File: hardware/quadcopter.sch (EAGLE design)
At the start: 61 parts, among them J1 AVR_SPI_PRG_6NS, J2 HEADER-4POS-2X2-0.1IN-FEMALE-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, J3 HEADER-10POSTH-254X10, J4 HEADER-4POS-0.1IN-FEMALE-SMD-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, Q1 MOSFET-SI2302CDS-T1-E3CT-ND, Q2 MOSFET-SI2302CDS-T1-E3CT-ND, Q3 MOSFET-SI2302CDS-T1-E3CT-ND, Q4 MOSFET-SI2302CDS-T1-E3CT-ND, Q5 MOSFET-SI2302CDS-T1-E3CT-ND, Q6 MOSFET-SI2302CDS-T1-E3CT-ND, SW1 PUSHBUTTON_SMD-VERTICAL-1, U1 ATMEGA128RFA1, U2 LSM-IMU-497-18367-1-NDIMU, Y1 CRYSTAL5X3

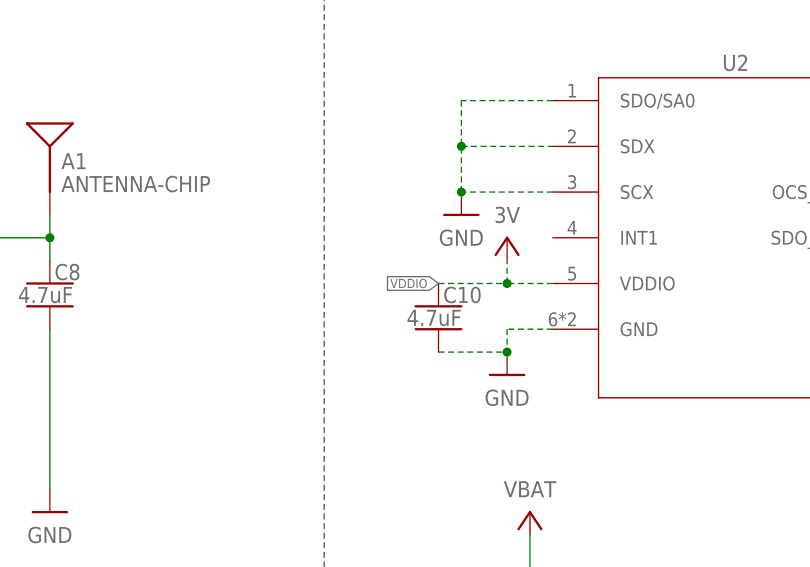
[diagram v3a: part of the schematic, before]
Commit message: switched gnd to gnd and removed VDDIO tag
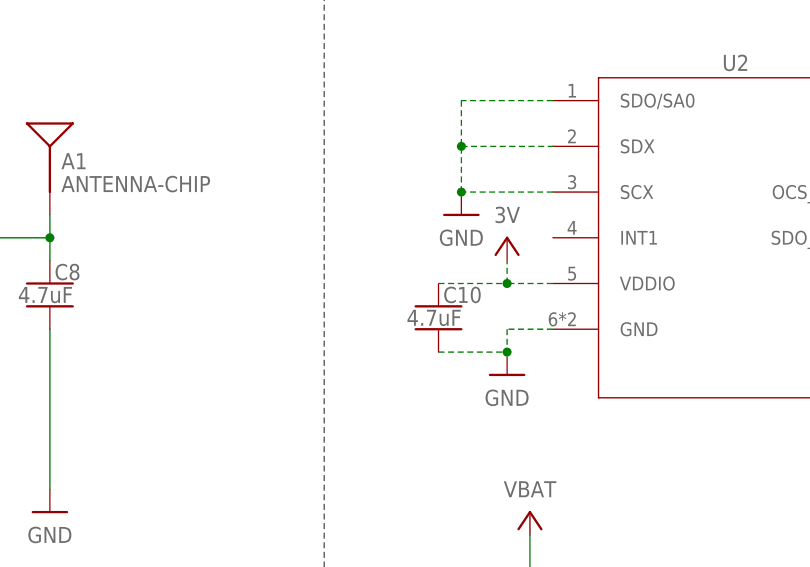
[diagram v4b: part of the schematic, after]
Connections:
- removed net GND1: C11.2
- net GND: now also C11.2
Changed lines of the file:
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@@
 <part name="P+7" library="quadparts_prebuilt_2022" deviceset="3V" device=""/>
 <part name="C10" library="quadparts_prebuilt_2022" deviceset="CAPACITOR-NP_" device="SMD-2012-0805_CERAMIC-4.7UF" value="4.7uF"/>
-<part name="GND19" library="quadparts_prebuilt_2022" deviceset="GND" device=""/>
 <part name="C11" library="quadparts_prebuilt_2022" deviceset="CAPACITOR-NP_" device="SMD-2012-0805_CERAMIC-4.7UF" value="4.7uF"/>
 <part name="R4" library="custom.lbr" library_urn="urn:adsk.wipprod:fs.file:vf.FjMADskDQ2Se9fX1PD5xcw" deviceset="MY-RESISTOR" device="-08050OHMRES" value="10k"/>
@@
 <part name="R12" library="custom.lbr" library_urn="urn:adsk.wipprod:fs.file:vf.FjMADskDQ2Se9fX1PD5xcw" deviceset="MY-RESISTOR" device="-08050OHMRES" value="2.2K"/>
 <part name="R14" library="custom.lbr" library_urn="urn:adsk.wipprod:fs.file:vf.FjMADskDQ2Se9fX1PD5xcw" deviceset="MY-RESISTOR" device="-08050OHMRES" value="2.2K"/>
+<part name="GND19" library="quadparts_prebuilt_2022" deviceset="GND" device=""/>
 </parts>
 <sheets>
@@
 <attribute name="NAME" x="229.108" y="150.241" size="1.778" layer="95"/>
 </instance>
-<instance part="GND19" gate="1" x="299.72" y="162.56" smashed="yes">
-<attribute name="VALUE" x="299.72" y="160.02" size="1.778" layer="96" align="center"/>
-</instance>
 <instance part="C11" gate="G$1" x="297.18" y="170.18" smashed="yes">
 <attribute name="VALUE" x="293.624" y="168.021" size="1.778" layer="96"/>
@@
 <attribute name="NAME" x="139.7" y="190.5" size="1.778" layer="95" rot="R90" align="bottom-center"/>
 <attribute name="VALUE" x="147.32" y="190.5" size="1.778" layer="96" rot="R90" align="bottom-center"/>
+</instance>
+<instance part="GND19" gate="1" x="299.72" y="162.56" smashed="yes">
+<attribute name="VALUE" x="299.72" y="160.02" size="1.778" layer="96" align="center"/>
 </instance>
 </instances>
@@
 <pinref part="C16" gate="G$1" pin="2"/>
 </segment>
+<segment>
+<wire x1="297.18" y1="165.1" x2="299.72" y2="165.1" width="0.1524" layer="91" style="longdash"/>
+<pinref part="C11" gate="G$1" pin="2"/>
+<pinref part="GND19" gate="1" pin="GND"/>
+</segment>
 </net>
 <net name="PG1" class="0">
@@
 </segment>
 </net>
-<net name="GND1" class="0">
-<segment>
-<wire x1="297.18" y1="165.1" x2="299.72" y2="165.1" width="0.1524" layer="91" style="longdash"/>
-<pinref part="GND19" gate="1" pin="GND"/>
-<pinref part="C11" gate="G$1" pin="2"/>
-</segment>
-</net>
 <net name="VDDIO" class="0">
 <segment>
@@
 <pinref part="P+5" gate="G$1" pin="3V"/>
 <wire x1="228.6" y1="152.4" x2="236.22" y2="152.4" width="0.1524" layer="91" style="longdash"/>
+<pinref part="C10" gate="G$1" pin="1"/>
 <junction x="236.22" y="152.4"/>
-<label x="228.6" y="152.4" size="1.016" layer="95" rot="R180" xref="yes"/>
-<pinref part="C10" gate="G$1" pin="1"/>
-</segment>
-<segment>
+</segment>
+<segment>

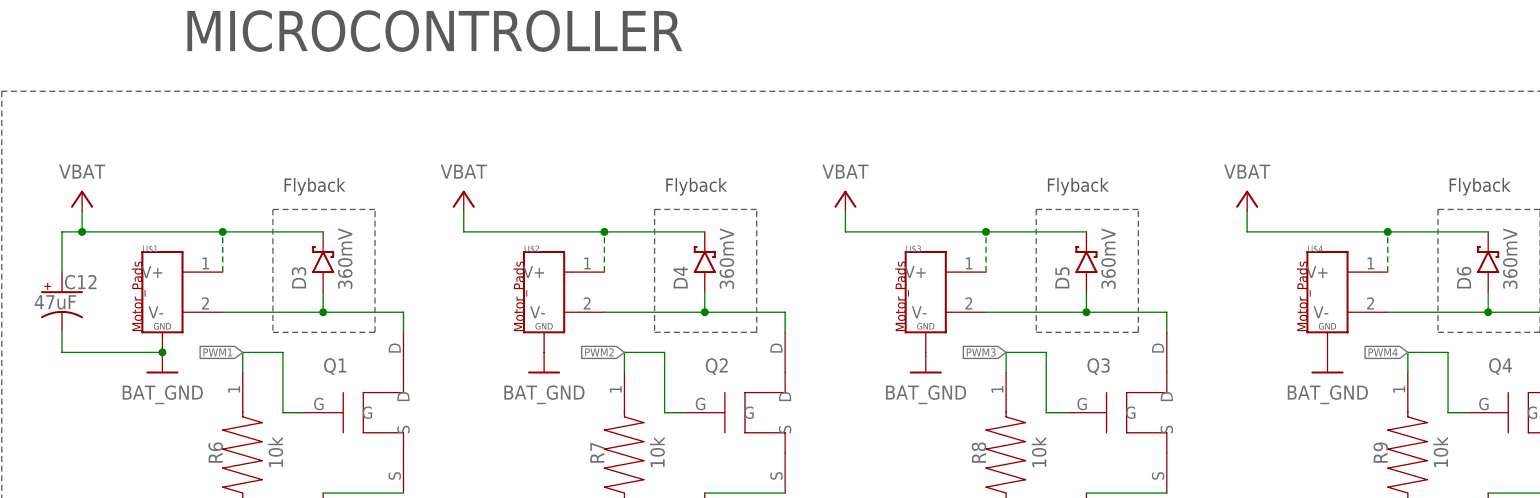
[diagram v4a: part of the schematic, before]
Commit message: renamed motors
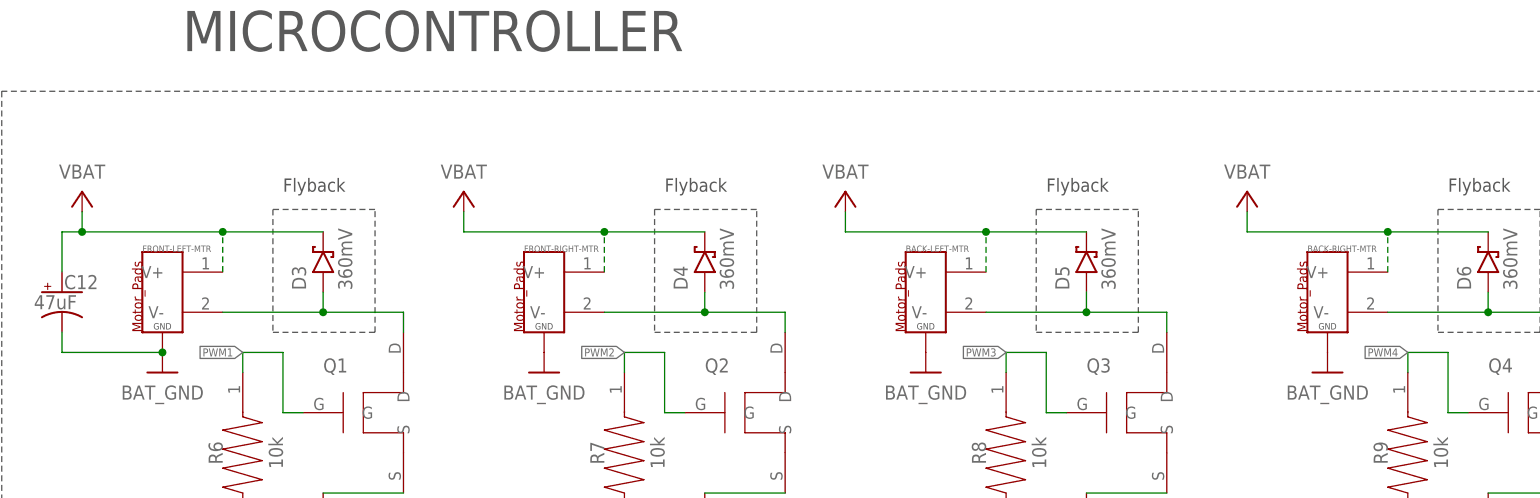
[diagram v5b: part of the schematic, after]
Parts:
- renumbered U$1 to FRONT-LEFT-MTR, U$2 to FRONT-RIGHT-MTR, U$3 to BACK-LEFT-MTR, U$4 to BACK-RIGHT-MTR
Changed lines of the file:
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@@
 <part name="R4" library="custom.lbr" library_urn="urn:adsk.wipprod:fs.file:vf.FjMADskDQ2Se9fX1PD5xcw" deviceset="MY-RESISTOR" device="-08050OHMRES" value="10k"/>
 <part name="R5" library="custom.lbr" library_urn="urn:adsk.wipprod:fs.file:vf.FjMADskDQ2Se9fX1PD5xcw" deviceset="MY-RESISTOR" device="-08050OHMRES" value="10k"/>
-<part name="U$1" library="quadparts_prebuilt_2022" deviceset="MOTOR_PADS_GND" device="-MOLEX-SMD"/>
+<part name="FRONT-LEFT-MTR" library="quadparts_prebuilt_2022" deviceset="MOTOR_PADS_GND" device="-MOLEX-SMD"/>
 <part name="P+8" library="quadparts_prebuilt_2022" deviceset="VBAT" device=""/>
 <part name="D3" library="quadparts_prebuilt_2022" deviceset="DIODE-SCHOTTKY_" device="-SMD-SOD123" package3d_urn="urn:adsk.eagle:package:11793366/1" value="360mV"/>
@@
 <part name="GND22" library="quadparts_prebuilt_2022" deviceset="GND" device=""/>
 <part name="Q1" library="custom.lbr" library_urn="urn:adsk.wipprod:fs.file:vf.FjMADskDQ2Se9fX1PD5xcw" deviceset="MOSFET" device="-SI2302CDS-T1-E3CT-ND"/>
-<part name="U$2" library="quadparts_prebuilt_2022" deviceset="MOTOR_PADS_GND" device="-MOLEX-SMD"/>
+<part name="FRONT-RIGHT-MTR" library="quadparts_prebuilt_2022" deviceset="MOTOR_PADS_GND" device="-MOLEX-SMD"/>
 <part name="P+9" library="quadparts_prebuilt_2022" deviceset="VBAT" device=""/>
 <part name="D4" library="quadparts_prebuilt_2022" deviceset="DIODE-SCHOTTKY_" device="-SMD-SOD123" package3d_urn="urn:adsk.eagle:package:11793366/1" value="360mV"/>
@@
 <part name="GND25" library="quadparts_prebuilt_2022" deviceset="GND" device=""/>
 <part name="Q2" library="custom.lbr" library_urn="urn:adsk.wipprod:fs.file:vf.FjMADskDQ2Se9fX1PD5xcw" deviceset="MOSFET" device="-SI2302CDS-T1-E3CT-ND"/>
-<part name="U$3" library="quadparts_prebuilt_2022" deviceset="MOTOR_PADS_GND" device="-MOLEX-SMD"/>
+<part name="BACK-LEFT-MTR" library="quadparts_prebuilt_2022" deviceset="MOTOR_PADS_GND" device="-MOLEX-SMD"/>
 <part name="P+10" library="quadparts_prebuilt_2022" deviceset="VBAT" device=""/>
 <part name="D5" library="quadparts_prebuilt_2022" deviceset="DIODE-SCHOTTKY_" device="-SMD-SOD123" package3d_urn="urn:adsk.eagle:package:11793366/1" value="360mV"/>
@@
 <part name="GND28" library="quadparts_prebuilt_2022" deviceset="GND" device=""/>
 <part name="Q3" library="custom.lbr" library_urn="urn:adsk.wipprod:fs.file:vf.FjMADskDQ2Se9fX1PD5xcw" deviceset="MOSFET" device="-SI2302CDS-T1-E3CT-ND"/>
-<part name="U$4" library="quadparts_prebuilt_2022" deviceset="MOTOR_PADS_GND" device="-MOLEX-SMD"/>
+<part name="BACK-RIGHT-MTR" library="quadparts_prebuilt_2022" deviceset="MOTOR_PADS_GND" device="-MOLEX-SMD"/>
 <part name="P+11" library="quadparts_prebuilt_2022" deviceset="VBAT" device=""/>
 <part name="D6" library="quadparts_prebuilt_2022" deviceset="DIODE-SCHOTTKY_" device="-SMD-SOD123" package3d_urn="urn:adsk.eagle:package:11793366/1" value="360mV"/>
@@
 <attribute name="VALUE" x="309.88" y="137.16" size="1.778" layer="96" align="bottom-center"/>
 </instance>
-<instance part="U$1" gate="G$1" x="7.62" y="27.94" smashed="yes">
+<instance part="FRONT-LEFT-MTR" gate="G$1" x="7.62" y="27.94" smashed="yes">
 <attribute name="NAME" x="5.08" y="35.56" size="0.8128" layer="95"/>
 </instance>
@@
 <attribute name="NAME" x="27.94" y="20.32" size="1.778" layer="95"/>
 </instance>
-<instance part="U$2" gate="G$1" x="55.88" y="27.94" smashed="yes">
+<instance part="FRONT-RIGHT-MTR" gate="G$1" x="55.88" y="27.94" smashed="yes">
 <attribute name="NAME" x="53.34" y="35.56" size="0.8128" layer="95"/>
 </instance>
@@
 <attribute name="NAME" x="76.2" y="20.32" size="1.778" layer="95"/>
 </instance>
-<instance part="U$3" gate="G$1" x="104.14" y="27.94" smashed="yes">
+<instance part="BACK-LEFT-MTR" gate="G$1" x="104.14" y="27.94" smashed="yes">
 <attribute name="NAME" x="101.6" y="35.56" size="0.8128" layer="95"/>
 </instance>
@@
 <attribute name="NAME" x="124.46" y="20.32" size="1.778" layer="95"/>
 </instance>
-<instance part="U$4" gate="G$1" x="154.94" y="27.94" smashed="yes">
+<instance part="BACK-RIGHT-MTR" gate="G$1" x="154.94" y="27.94" smashed="yes">
 <attribute name="NAME" x="152.4" y="35.56" size="0.8128" layer="95"/>
 </instance>
@@
 <net name="VBAT" class="0">
 <segment>
-<pinref part="U$1" gate="G$1" pin="V+"/>
+<pinref part="FRONT-LEFT-MTR" gate="G$1" pin="V+"/>
 <wire x1="15.24" y1="33.02" x2="15.24" y2="38.1" width="0.1524" layer="91" style="longdash"/>
 <wire x1="15.24" y1="38.1" x2="-2.54" y2="38.1" width="0.1524" layer="91"/>
@@
 </segment>
 <segment>
-<pinref part="U$2" gate="G$1" pin="V+"/>
+<pinref part="FRONT-RIGHT-MTR" gate="G$1" pin="V+"/>
 <wire x1="63.5" y1="33.02" x2="63.5" y2="38.1" width="0.1524" layer="91" style="longdash"/>
 <wire x1="63.5" y1="38.1" x2="45.72" y2="38.1" width="0.1524" layer="91"/>
@@
 </segment>
 <segment>
-<pinref part="U$3" gate="G$1" pin="V+"/>
+<pinref part="BACK-LEFT-MTR" gate="G$1" pin="V+"/>
 <wire x1="111.76" y1="33.02" x2="111.76" y2="38.1" width="0.1524" layer="91" style="longdash"/>
 <wire x1="111.76" y1="38.1" x2="93.98" y2="38.1" width="0.1524" layer="91"/>
@@
 </segment>
 <segment>
-<pinref part="U$4" gate="G$1" pin="V+"/>
+<pinref part="BACK-RIGHT-MTR" gate="G$1" pin="V+"/>
 <wire x1="162.56" y1="33.02" x2="162.56" y2="38.1" width="0.1524" layer="91" style="longdash"/>
 <wire x1="162.56" y1="38.1" x2="144.78" y2="38.1" width="0.1524" layer="91"/>
@@
 <wire x1="27.94" y1="30.48" x2="27.94" y2="27.94" width="0.1524" layer="91"/>
 <wire x1="27.94" y1="27.94" x2="15.24" y2="27.94" width="0.1524" layer="91"/>
-<pinref part="U$1" gate="G$1" pin="V-"/>
+<pinref part="FRONT-LEFT-MTR" gate="G$1" pin="V-"/>
 <wire x1="27.94" y1="27.94" x2="38.1" y2="27.94" width="0.1524" layer="91"/>
 <junction x="27.94" y="27.94"/>
@@
 <net name="BAT_GND" class="0">
 <segment>
-<pinref part="U$1" gate="G$1" pin="GND"/>
+<pinref part="FRONT-LEFT-MTR" gate="G$1" pin="GND"/>
 <pinref part="GND20" gate="1" pin="BAT_GND"/>
 <wire x1="-5.08" y1="25.4" x2="-5.08" y2="22.86" width="0.1524" layer="91"/>
@@
 </segment>
 <segment>
-<pinref part="U$2" gate="G$1" pin="GND"/>
+<pinref part="FRONT-RIGHT-MTR" gate="G$1" pin="GND"/>
 <pinref part="GND23" gate="1" pin="BAT_GND"/>
 </segment>
@@
 </segment>
 <segment>
-<pinref part="U$3" gate="G$1" pin="GND"/>
+<pinref part="BACK-LEFT-MTR" gate="G$1" pin="GND"/>
 <pinref part="GND26" gate="1" pin="BAT_GND"/>
 </segment>
@@
 </segment>
 <segment>
-<pinref part="U$4" gate="G$1" pin="GND"/>
+<pinref part="BACK-RIGHT-MTR" gate="G$1" pin="GND"/>
 <pinref part="GND29" gate="1" pin="BAT_GND"/>
 </segment>
@@
 <wire x1="76.2" y1="30.48" x2="76.2" y2="27.94" width="0.1524" layer="91"/>
 <wire x1="76.2" y1="27.94" x2="63.5" y2="27.94" width="0.1524" layer="91"/>
-<pinref part="U$2" gate="G$1" pin="V-"/>
+<pinref part="FRONT-RIGHT-MTR" gate="G$1" pin="V-"/>
 <wire x1="76.2" y1="27.94" x2="86.36" y2="27.94" width="0.1524" layer="91"/>
 <junction x="76.2" y="27.94"/>
@@
 <wire x1="124.46" y1="30.48" x2="124.46" y2="27.94" width="0.1524" layer="91"/>
 <wire x1="124.46" y1="27.94" x2="111.76" y2="27.94" width="0.1524" layer="91"/>
-<pinref part="U$3" gate="G$1" pin="V-"/>
+<pinref part="BACK-LEFT-MTR" gate="G$1" pin="V-"/>
 <wire x1="124.46" y1="27.94" x2="134.62" y2="27.94" width="0.1524" layer="91"/>
 <junction x="124.46" y="27.94"/>
@@
 <wire x1="175.26" y1="30.48" x2="175.26" y2="27.94" width="0.1524" layer="91"/>
 <wire x1="175.26" y1="27.94" x2="162.56" y2="27.94" width="0.1524" layer="91"/>
-<pinref part="U$4" gate="G$1" pin="V-"/>
+<pinref part="BACK-RIGHT-MTR" gate="G$1" pin="V-"/>
 <wire x1="175.26" y1="27.94" x2="185.42" y2="27.94" width="0.1524" layer="91"/>
 <junction x="175.26" y="27.94"/>

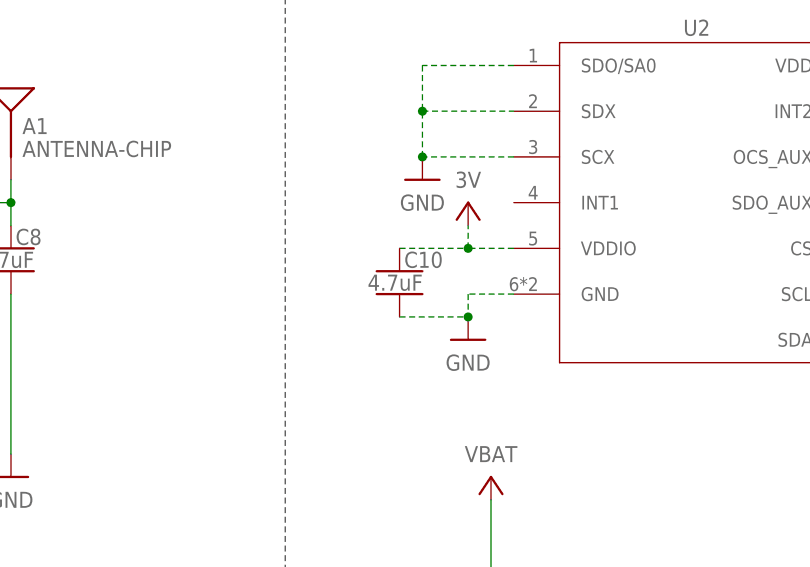
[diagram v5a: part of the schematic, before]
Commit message: fixed vddio capacitance
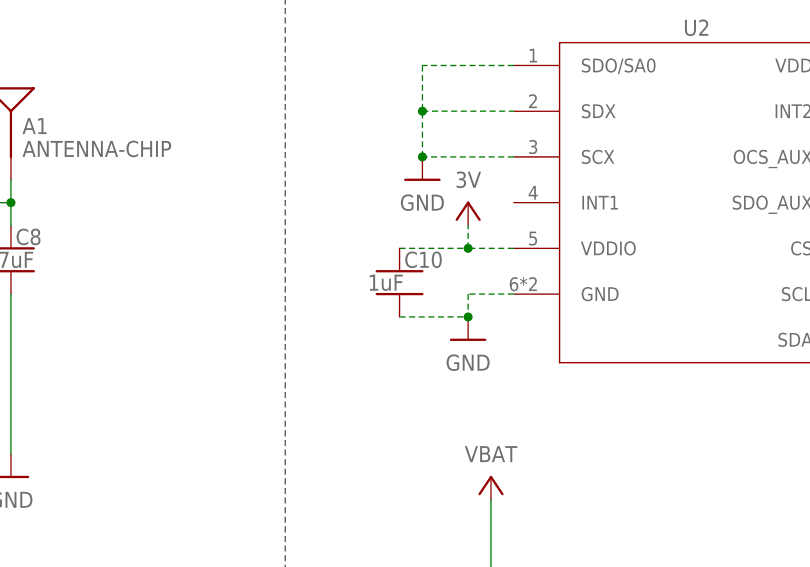
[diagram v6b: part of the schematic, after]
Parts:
- C10: value 4.7uF -> 1uF
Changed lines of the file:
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@@
 <part name="GND18" library="quadparts_prebuilt_2022" deviceset="GND" device=""/>
 <part name="P+7" library="quadparts_prebuilt_2022" deviceset="3V" device=""/>
-<part name="C10" library="quadparts_prebuilt_2022" deviceset="CAPACITOR-NP_" device="SMD-2012-0805_CERAMIC-4.7UF" value="4.7uF"/>
+<part name="C10" library="quadparts_prebuilt_2022" deviceset="CAPACITOR-NP_" device="SMD-2012-0805_CERAMIC-4.7UF" value="1uF"/>
 <part name="C11" library="quadparts_prebuilt_2022" deviceset="CAPACITOR-NP_" device="SMD-2012-0805_CERAMIC-4.7UF" value="4.7uF"/>
 <part name="R4" library="custom.lbr" library_urn="urn:adsk.wipprod:fs.file:vf.FjMADskDQ2Se9fX1PD5xcw" deviceset="MY-RESISTOR" device="-08050OHMRES" value="10k"/>

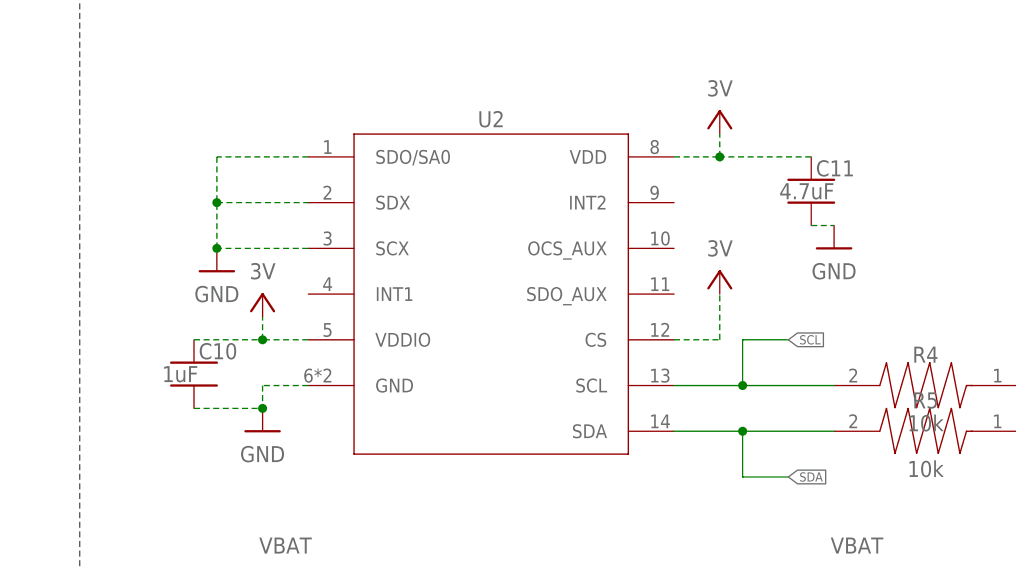
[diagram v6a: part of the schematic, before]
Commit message: IMU capacitances fixed?
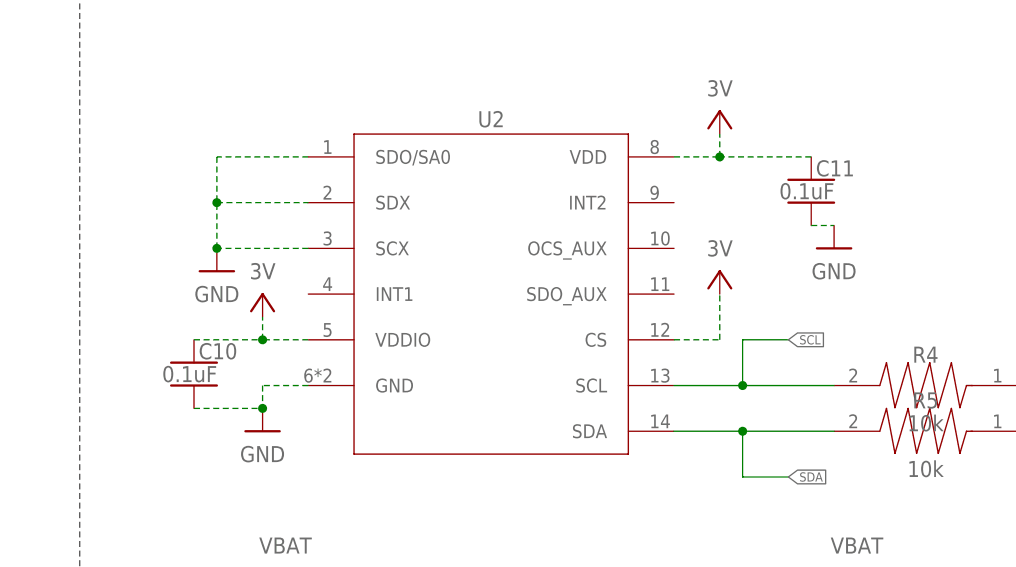
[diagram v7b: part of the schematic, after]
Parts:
- C10: value 1uF -> 0.1uF
- C11: value 4.7uF -> 0.1uF
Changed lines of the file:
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@@
 <part name="GND18" library="quadparts_prebuilt_2022" deviceset="GND" device=""/>
 <part name="P+7" library="quadparts_prebuilt_2022" deviceset="3V" device=""/>
-<part name="C10" library="quadparts_prebuilt_2022" deviceset="CAPACITOR-NP_" device="SMD-2012-0805_CERAMIC-4.7UF" value="1uF"/>
-<part name="C11" library="quadparts_prebuilt_2022" deviceset="CAPACITOR-NP_" device="SMD-2012-0805_CERAMIC-4.7UF" value="4.7uF"/>
+<part name="C10" library="quadparts_prebuilt_2022" deviceset="CAPACITOR-NP_" device="SMD-2012-0805_CERAMIC-4.7UF" value="0.1uF"/>
+<part name="C11" library="quadparts_prebuilt_2022" deviceset="CAPACITOR-NP_" device="SMD-2012-0805_CERAMIC-4.7UF" value="0.1uF"/>
 <part name="R4" library="custom.lbr" library_urn="urn:adsk.wipprod:fs.file:vf.FjMADskDQ2Se9fX1PD5xcw" deviceset="MY-RESISTOR" device="-08050OHMRES" value="10k"/>
 <part name="R5" library="custom.lbr" library_urn="urn:adsk.wipprod:fs.file:vf.FjMADskDQ2Se9fX1PD5xcw" deviceset="MY-RESISTOR" device="-08050OHMRES" value="10k"/>
